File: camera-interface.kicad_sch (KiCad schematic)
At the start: 44 parts, among them J7 WE_68715014522

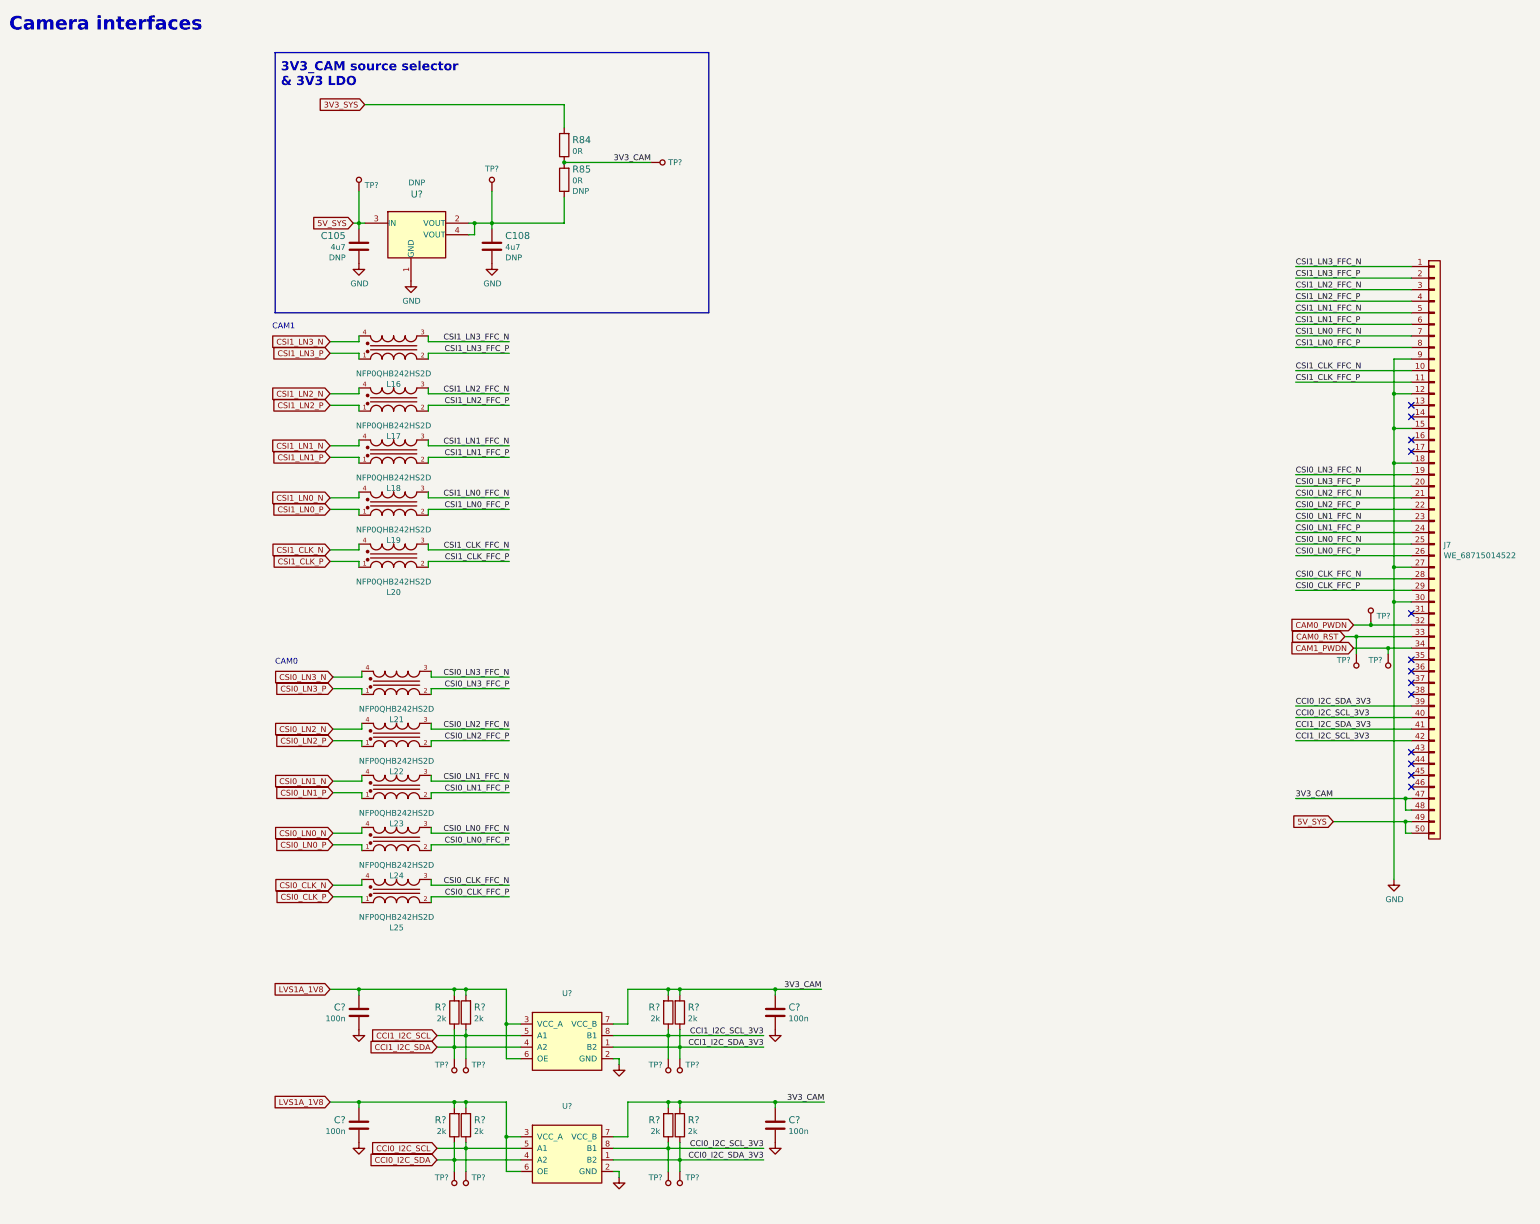
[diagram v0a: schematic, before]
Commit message: Introduce component standardization
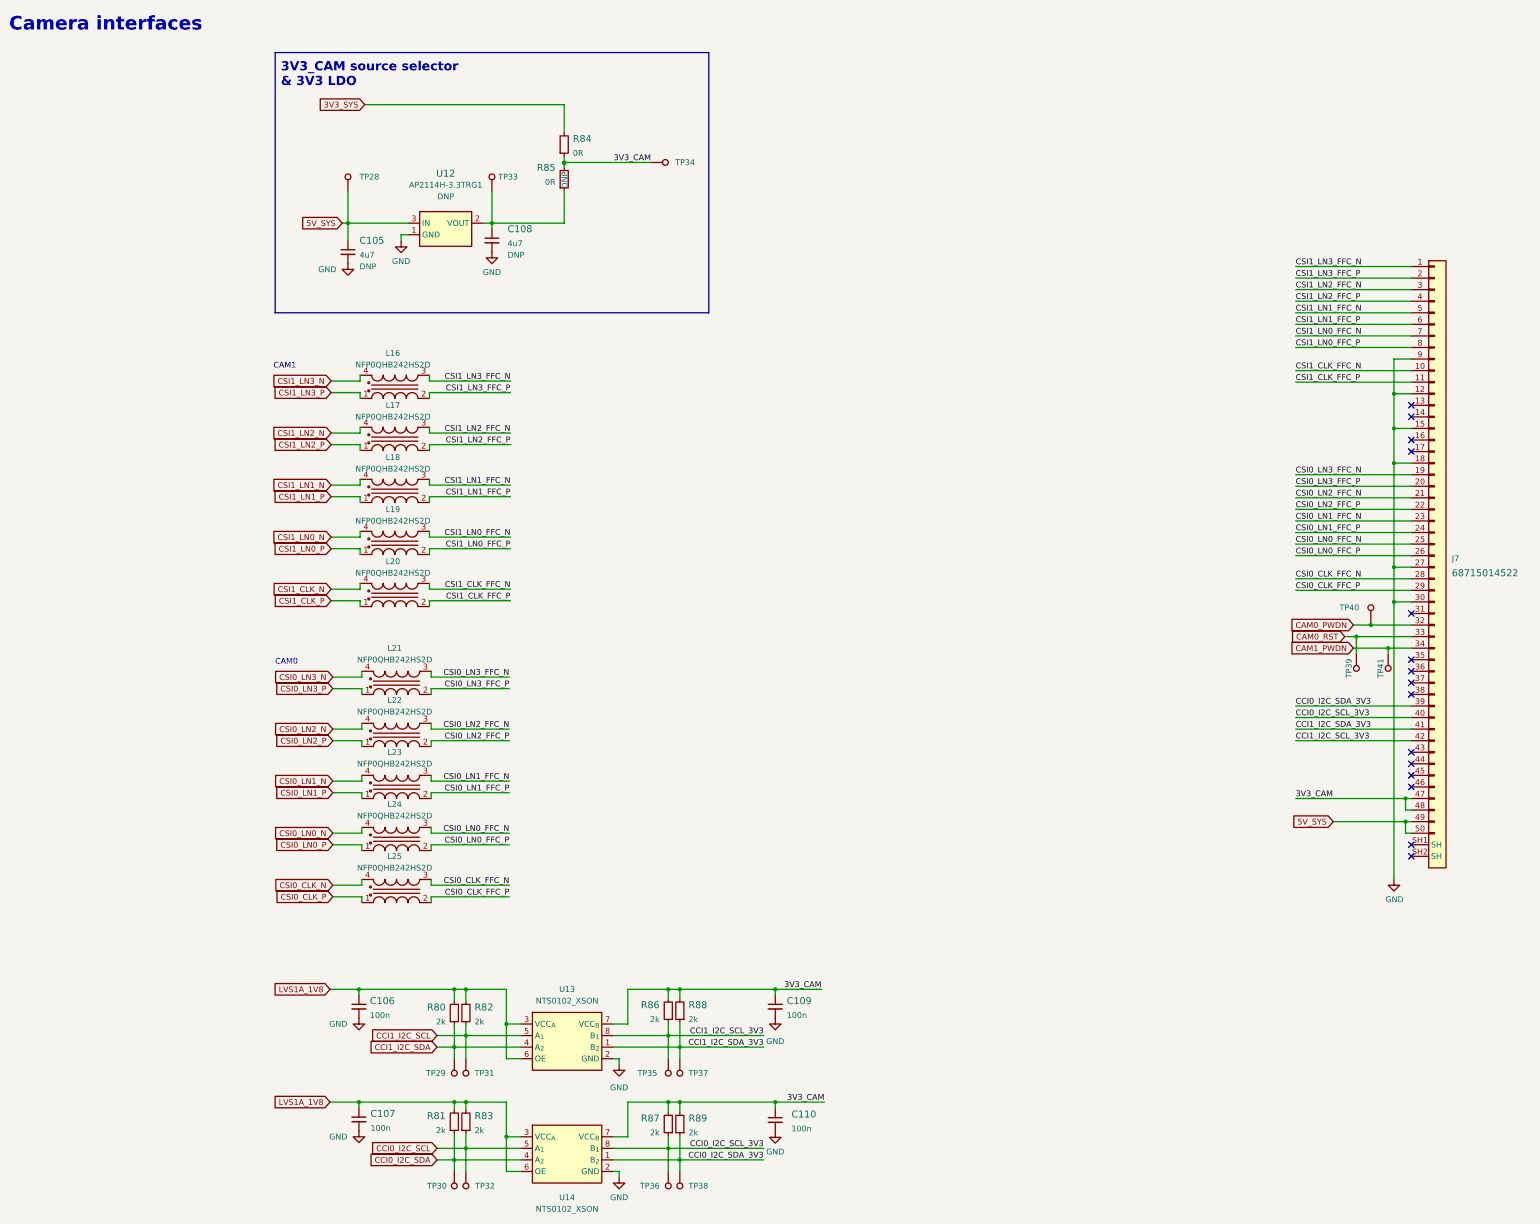
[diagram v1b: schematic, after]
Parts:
- C105, C108: footprint sa800u-baseboard-hw-footprints:0805-cap -> sa800u-baseboard-hw-footprints:C_0805_2012Metric; Author (none) -> Antmicro; License (none) -> Apache-2.0; Manufacturer WALSIN -> Walsin
- C106, C107, C109, C110: renamed from C?; value (none) -> C_100n_0402; footprint (none) -> sa800u-baseboard-hw-footprints:C_0402_1005Metric; Author (none) -> Antmicro; Dielectric (none) -> X5R; License (none) -> Apache-2.0; Voltage (none) -> 50V
- J7: value WE_68715014522 -> Conn_FFC_WE_68715014522_TWO-SIDES; footprint sa800u-baseboard-hw-footprints:WE_68715014522 -> sa800u-baseboard-hw-footprints:Conn_FFC_WE_68715014x22_ALT; symbol sa800u-baseboard-hw:WE_68715014522 -> sa800u-baseboard-hw:Conn_FFC_WE_68715014522_TWO-SIDES; Author (none) -> Antmicro; License (none) -> Apache-2.0; MPN 68715014522 -> 68715014522; Manufacturer Wurth Elektronik -> Würth Elektronik
- L16, L17, L18, L19, L20, L21, L22, L23, L24, L25: footprint sa800u-baseboard-hw-footprints:FIL_NFP0QHB242HS2D -> sa800u-baseboard-hw-footprints:L_Murata_025020_0605Metric; Author (none) -> Antmicro; License (none) -> Apache-2.0; Manufacturer MURATA -> Murata
- R80, R81, R82, R83, R86, R87, R88, R89: renamed from R?; value (none) -> R_2k_0402; footprint (none) -> sa800u-baseboard-hw-footprints:R_0402_1005Metric; Author (none) -> Antmicro; License (none) -> Apache-2.0; MPN CRCW04022K00FKED -> CR0402-FX-2001GLF; Manufacturer VISHAY -> Bourns; Tolerance (none) -> 1%
- R84, R85: footprint sa800u-baseboard-hw-footprints:0603-res -> sa800u-baseboard-hw-footprints:R_0603_1608Metric; Author (none) -> Antmicro; Current (none) -> 1A; License (none) -> Apache-2.0; Manufacturer BOURNS -> Bourns
- TP28, TP29, TP30, TP31, TP32, TP33, TP34, TP35, TP36, TP37, TP38, TP39, TP40, TP41: renamed from TP?; value (none) -> TP_0.75mm_SMD; footprint (none) -> sa800u-baseboard-hw-footprints:TP_SMD_0.75mm; symbol sa800u-baseboard-hw:TP_SMD_0_75MM -> sa800u-baseboard-hw:TP_0.75mm_SMD; Author (none) -> Antmicro; License (none) -> Apache-2.0
- U12: renamed from U?; value (none) -> AP2114H-3.3TRG1; footprint (none) -> sa800u-baseboard-hw-footprints:SOT-223; symbol sa800u-baseboard-hw:AP2114H-3_3TRG1 -> sa800u-baseboard-hw:AP2114H-3.3TRG1; Author (none) -> Antmicro; License (none) -> Apache-2.0
- U13, U14: renamed from U?; value (none) -> NTS0102_XSON; footprint (none) -> sa800u-baseboard-hw-footprints:XSON-8_1x1.95mm_P0.5mm; symbol sa800u-baseboard-hw:NTS0102GT -> sa800u-baseboard-hw:NTS0102_XSON; Author (none) -> Antmicro; License (none) -> Apache-2.0; Manufacturer NXP Semiconductors -> NXP
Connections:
- no-connect marks 13 -> 15
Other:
- moved on the sheet: C105, C106, C107, C108, C109, C110, L16, L17, L18, L19, L20, R81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

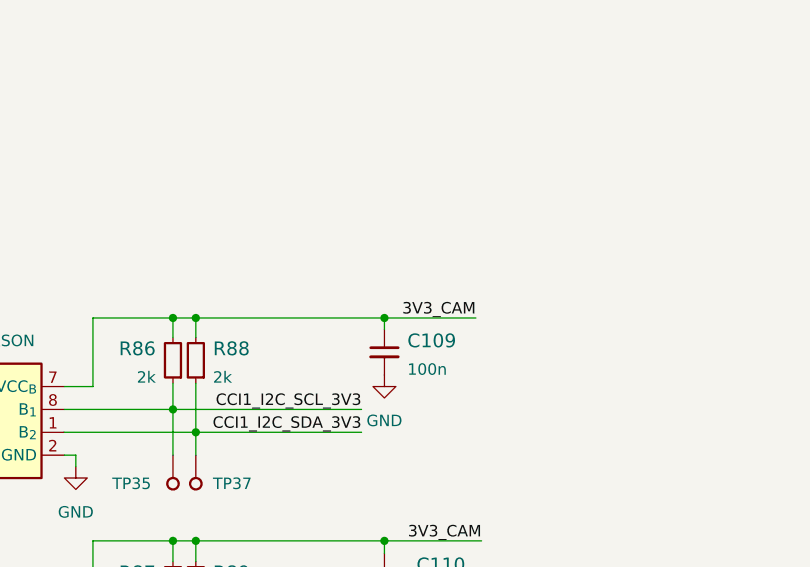
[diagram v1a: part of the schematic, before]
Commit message: Add OHP assets
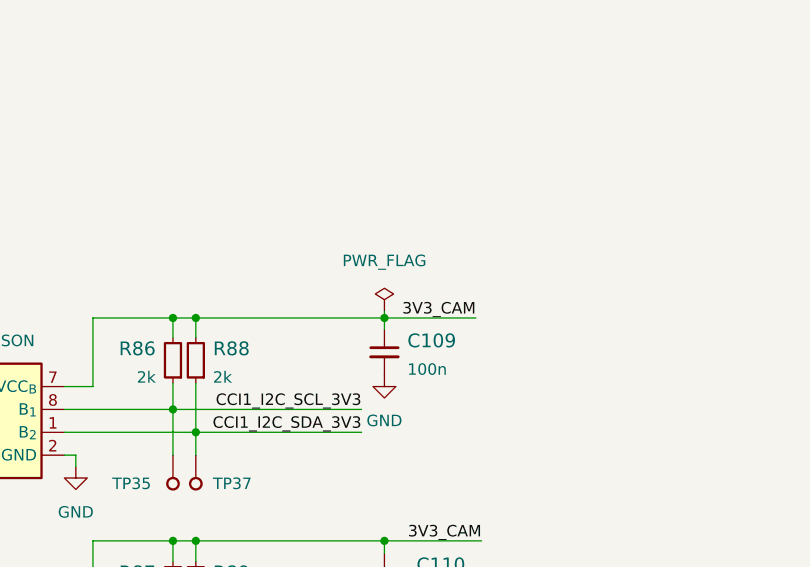
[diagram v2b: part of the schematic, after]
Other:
- company: (none) -> Antmicro Ltd.
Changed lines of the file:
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@@
   (title_block
     (title "SA800U (Snapdragon 845) Baseboard")
-    (date "2023-07-27")
-    (rev "1.0.2")
+    (date "2023-10-19")
+    (rev "1.0.3")
+    (company "Antmicro Ltd.")
     (comment 1 "www.antmicro.com")
-    (comment 2 "Antmicro Ltd.")
   )
   (junction (at 122.555 236.22) (diameter 0) (color 0 0 0 0)
@@
     (stroke (width 0) (type default) (color 0 0 0 0))
   )
+  (wire (pts (xy 181.61 227.838) (xy 181.61 228.6))
+    (stroke (width 0) (type default) (color 0 0 0 0))
+  )
   (wire (pts (xy 106.045 196.85) (xy 123.19 196.85))
     (stroke (width 0) (type default) (color 0 0 0 0))
@@
     (stroke (width 0) (type default) (color 0 0 0 0))
   )
-  (wire (pts (xy 191.77 228.6) (xy 181.61 228.6))
-    (stroke (width 0) (type default) (color 0 0 0 0))
-  )
   (wire (pts (xy 106.045 204.47) (xy 106.045 205.74))
     (stroke (width 0) (type default) (color 0 0 0 0))
@@
     (stroke (width 0) (type default) (color 0 0 0 0))
   )
+  (wire (pts (xy 181.61 228.6) (xy 191.77 228.6))
+    (stroke (width 0) (type default) (color 0 0 0 0))
+  )
   (wire (pts (xy 106.045 182.88) (xy 123.19 182.88))
     (stroke (width 0) (type default) (color 0 0 0 0))
@@
     (pin "1")
   )
-  (symbol (lib_id "sa800u-baseboard-hw:NFP0QHB242HS2D") (at 90.424 98.806 0) (mirror x) (unit 1)
+  (symbol (lib_name "NFP0QHB242HS2D_7") (lib_id "sa800u-baseboard-hw:NFP0QHB242HS2D") (at 90.424 98.806 0) (mirror x) (unit 1)
     (in_bom yes) (on_board yes) (fields_autoplaced)
     (property "Reference" "L16" (id 0) (at 97.6249 88.9 0))
@@
     (pin "4")
   )
-  (symbol (lib_id "sa800u-baseboard-hw:NFP0QHB242HS2D") (at 90.424 110.236 0) (mirror x) (unit 1)
+  (symbol (lib_name "NFP0QHB242HS2D_6") (lib_id "sa800u-baseboard-hw:NFP0QHB242HS2D") (at 90.424 110.236 0) (mirror x) (unit 1)
     (in_bom yes) (on_board yes) (fields_autoplaced)
     (property "Reference" "L17" (id 0) (at 97.6249 100.33 0))
@@
     (pin "4")
   )
-  (symbol (lib_id "sa800u-baseboard-hw:NFP0QHB242HS2D") (at 90.424 133.096 0) (mirror x) (unit 1)
+  (symbol (lib_name "NFP0QHB242HS2D_9") (lib_id "sa800u-baseboard-hw:NFP0QHB242HS2D") (at 90.424 133.096 0) (mirror x) (unit 1)
     (in_bom yes) (on_board yes) (fields_autoplaced)
     (property "Reference" "L19" (id 0) (at 97.6249 123.19 0))
@@
     (pin "4")
   )
-  (symbol (lib_id "sa800u-baseboard-hw:NFP0QHB242HS2D") (at 90.424 144.526 0) (mirror x) (unit 1)
+  (symbol (lib_name "NFP0QHB242HS2D_8") (lib_id "sa800u-baseboard-hw:NFP0QHB242HS2D") (at 90.424 144.526 0) (mirror x) (unit 1)
     (in_bom yes) (on_board yes) (fields_autoplaced)
     (property "Reference" "L20" (id 0) (at 97.6249 134.62 0))
@@
     (pin "4")
   )
-  (symbol (lib_id "sa800u-baseboard-hw:NFP0QHB242HS2D") (at 90.805 163.83 0) (mirror x) (unit 1)
+  (symbol (lib_name "NFP0QHB242HS2D_3") (lib_id "sa800u-baseboard-hw:NFP0QHB242HS2D") (at 90.805 163.83 0) (mirror x) (unit 1)
     (in_bom yes) (on_board yes) (fields_autoplaced)
     (property "Reference" "L21" (id 0) (at 98.0059 153.67 0))
@@
     (pin "4")
   )
-  (symbol (lib_id "sa800u-baseboard-hw:NFP0QHB242HS2D") (at 90.805 175.26 0) (mirror x) (unit 1)
+  (symbol (lib_name "NFP0QHB242HS2D_5") (lib_id "sa800u-baseboard-hw:NFP0QHB242HS2D") (at 90.805 175.26 0) (mirror x) (unit 1)
     (in_bom yes) (on_board yes) (fields_autoplaced)
     (property "Reference" "L22" (id 0) (at 98.0059 165.1 0))
@@
     (pin "4")
   )
-  (symbol (lib_id "sa800u-baseboard-hw:NFP0QHB242HS2D") (at 90.805 186.69 0) (mirror x) (unit 1)
+  (symbol (lib_name "NFP0QHB242HS2D_4") (lib_id "sa800u-baseboard-hw:NFP0QHB242HS2D") (at 90.805 186.69 0) (mirror x) (unit 1)
     (in_bom yes) (on_board yes) (fields_autoplaced)
     (property "Reference" "L23" (id 0) (at 98.0059 176.53 0))
@@
     (pin "4")
   )
-  (symbol (lib_id "sa800u-baseboard-hw:NFP0QHB242HS2D") (at 90.805 198.12 0) (mirror x) (unit 1)
+  (symbol (lib_name "NFP0QHB242HS2D_1") (lib_id "sa800u-baseboard-hw:NFP0QHB242HS2D") (at 90.805 198.12 0) (mirror x) (unit 1)
     (in_bom yes) (on_board yes) (fields_autoplaced)
     (property "Reference" "L24" (id 0) (at 98.0059 187.96 0))
@@
     (pin "4")
   )
-  (symbol (lib_id "sa800u-baseboard-hw:NFP0QHB242HS2D") (at 90.805 209.55 0) (mirror x) (unit 1)
+  (symbol (lib_name "NFP0QHB242HS2D_2") (lib_id "sa800u-baseboard-hw:NFP0QHB242HS2D") (at 90.805 209.55 0) (mirror x) (unit 1)
     (in_bom yes) (on_board yes) (fields_autoplaced)
     (property "Reference" "L25" (id 0) (at 98.0059 199.39 0))
@@
     )
     (pin "1")
+  )
+  (symbol (lib_id "sa800u-baseboard-hw:PWR_FLAG") (at 181.61 227.838 0) (unit 1)
+    (in_bom yes) (on_board yes)
+    (property "Reference" "#FLG0104" (id 0) (at 181.61 225.933 0)
+      (effects (font (size 1.27 1.27)) hide)
+    )
+    (property "Value" "PWR_FLAG" (id 1) (at 181.61 222.25 0))
+    (property "Footprint" "" (id 2) (at 181.61 227.838 0)
+      (effects (font (size 1.27 1.27)) hide)
+    )
+    (property "Datasheet" "~" (id 3) (at 181.61 227.838 0)
+      (effects (font (size 1.27 1.27)) hide)
+    )
+    (pin "1")
